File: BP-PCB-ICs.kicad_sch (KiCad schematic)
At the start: 40 parts, among them Q1 SSM6K514NU,LF, Q2 SSM6K514NU,LF, Q3 SSM6K514NU,LF, Q4 SSM6K514NU,LF, Q5 SSM6K514NU,LF, Q6 SSM6K514NU,LF, U1 LTC4361CTS8-2TRMPBF, U2 LTC4361CTS8-2TRMPBF, U4 LTC4380IDD-4-PBF, U6 LTC4380IDD-4-PBF

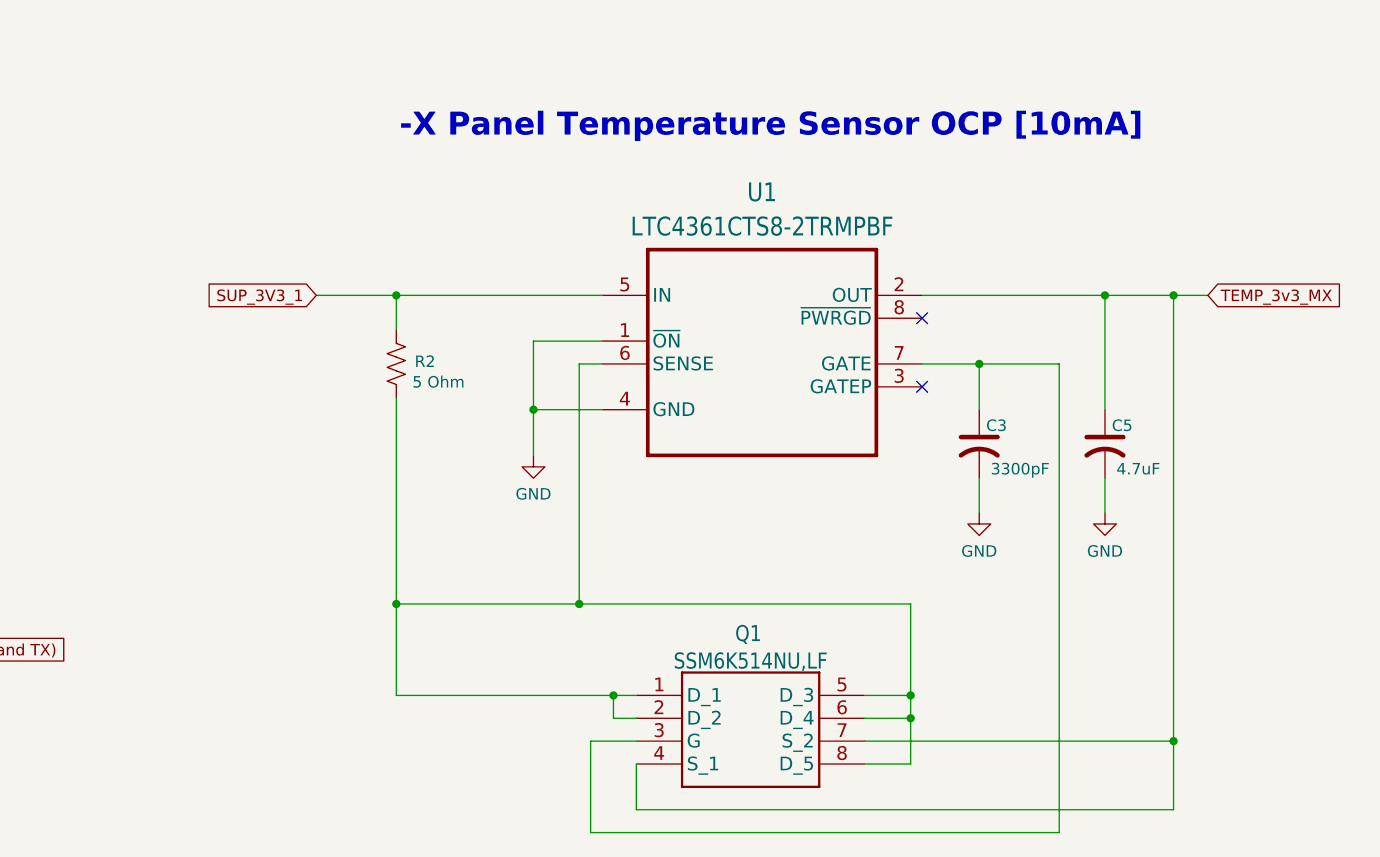
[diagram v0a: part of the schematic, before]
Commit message: -X temp OCP is being shared with BP
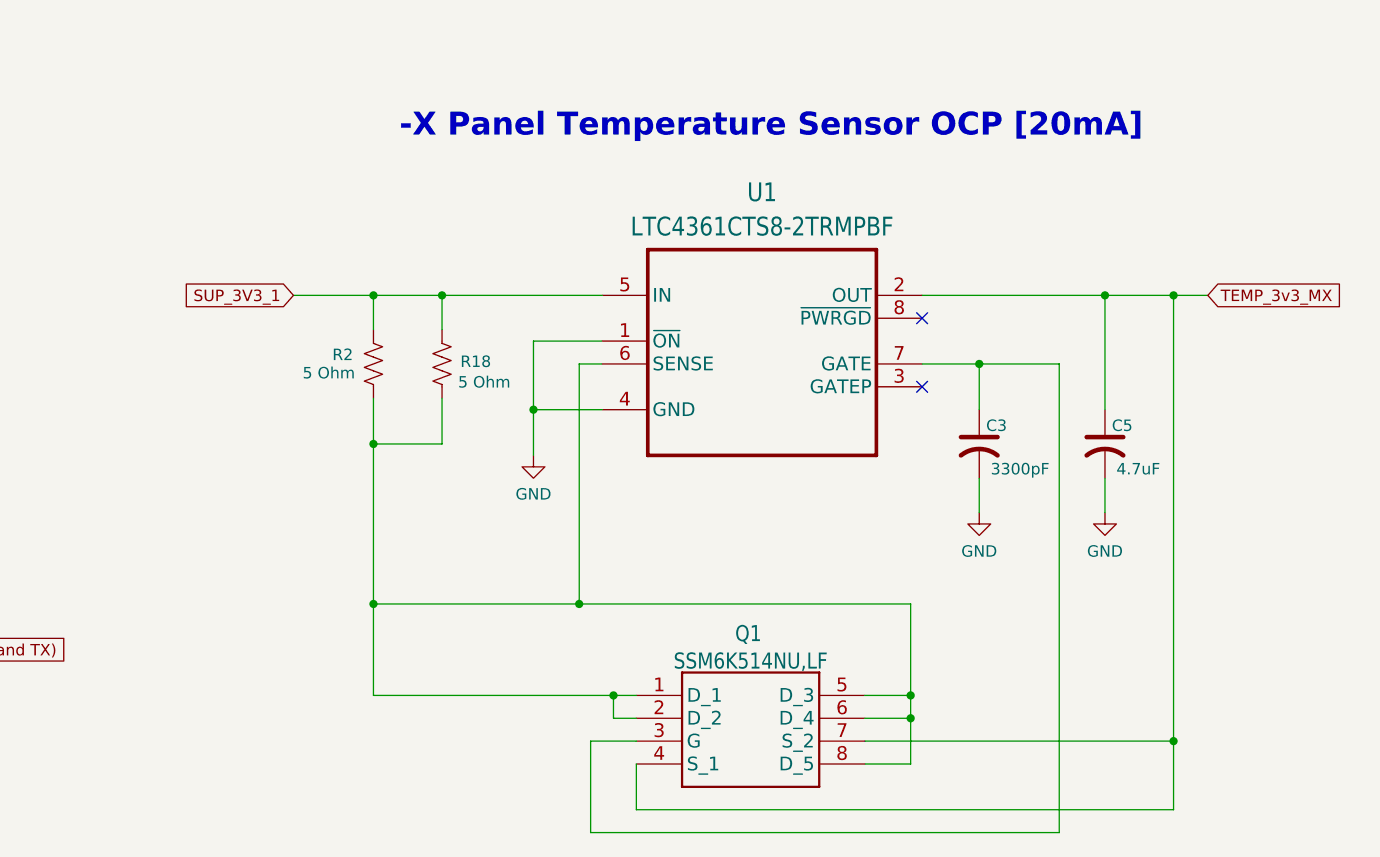
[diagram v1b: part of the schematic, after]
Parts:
- added R18: 5 Ohm, Resistor_SMD:R_0805_2012Metric, symbol Device:R_US
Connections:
- net SUP_3V3_1: now also R18.1
- net at Q1.1 (D_1), Q1.2 (D_2), Q1.5 (D_3)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: now also R18.2
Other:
- note added: "-X Panel Temperature Sensor OCP [20mA]"
- note removed: "-X Panel Temperature Sensor OCP [10mA]"
- moved on the sheet: R2
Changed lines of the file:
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@@
 		)
 	)
-	(text "-X Panel Temperature Sensor OCP [10mA]"
+	(text "-X Panel Temperature Sensor OCP [20mA]"
 		(exclude_from_sim no)
 		(at 329.946 32.004 0)
@@
 	)
 	(junction
+		(at 285.75 85.09)
+		(diameter 0)
+		(color 0 0 0 0)
+	)
+	(junction
 		(at 181.61 201.93)
 		(diameter 0)
@@
 	)
 	(junction
+		(at 293.37 50.8)
+		(diameter 0)
+		(color 0 0 0 0)
+	)
+	(junction
 		(at 345.44 198.12)
 		(diameter 0)
@@
 	)
 	(junction
-		(at 288.29 85.09)
-		(diameter 0)
-		(color 0 0 0 0)
-	)
-	(junction
 		(at 175.26 39.37)
 		(diameter 0)
@@
 	)
 	(junction
+		(at 285.75 50.8)
+		(diameter 0)
+		(color 0 0 0 0)
+	)
+	(junction
 		(at 288.29 153.67)
 		(diameter 0)
@@
 	)
 	(junction
-		(at 288.29 50.8)
-		(diameter 0)
-		(color 0 0 0 0)
-	)
-	(junction
 		(at 140.97 171.45)
 		(diameter 0)
@@
 		(color 0 0 0 0)
 	)
+	(junction
+		(at 285.75 67.31)
+		(diameter 0)
+		(color 0 0 0 0)
+	)
 	(no_connect
 		(at 346.71 60.96)
@@
 	(wire
 		(pts
+			(xy 285.75 50.8) (xy 293.37 50.8)
+		)
+		(stroke
+			(width 0)
+			(type default)
+		)
+	)
+	(wire
+		(pts
 			(xy 55.88 29.21) (xy 55.88 40.64)
 		)
@@
 	(wire
 		(pts
+			(xy 285.75 67.31) (xy 285.75 85.09)
+		)
+		(stroke
+			(width 0)
+			(type default)
+		)
+	)
+	(wire
+		(pts
 			(xy 176.53 151.13) (xy 176.53 156.21)
 		)
@@
 	(wire
 		(pts
-			(xy 288.29 95.25) (xy 312.42 95.25)
+			(xy 285.75 95.25) (xy 312.42 95.25)
 		)
 		(stroke
@@
 	(wire
 		(pts
-			(xy 288.29 85.09) (xy 288.29 95.25)
+			(xy 285.75 85.09) (xy 285.75 95.25)
 		)
 		(stroke
@@
 	(wire
 		(pts
-			(xy 288.29 50.8) (xy 311.15 50.8)
-		)
-		(stroke
-			(width 0)
-			(type default)
-		)
-	)
-	(wire
-		(pts
 			(xy 172.72 41.91) (xy 172.72 48.26)
 		)
@@
 	(wire
 		(pts
-			(xy 279.4 50.8) (xy 288.29 50.8)
+			(xy 276.86 50.8) (xy 285.75 50.8)
 		)
 		(stroke
@@
 	(wire
 		(pts
-			(xy 140.97 153.67) (xy 140.97 171.45)
+			(xy 293.37 62.23) (xy 293.37 67.31)
 		)
 		(stroke
@@
 	(wire
 		(pts
-			(xy 97.79 184.15) (xy 105.41 184.15)
+			(xy 140.97 153.67) (xy 140.97 171.45)
 		)
 		(stroke
@@
 	(wire
 		(pts
-			(xy 308.61 85.09) (xy 288.29 85.09)
+			(xy 97.79 184.15) (xy 105.41 184.15)
 		)
 		(stroke
@@
 	(wire
 		(pts
-			(xy 288.29 50.8) (xy 288.29 54.61)
-		)
-		(stroke
-			(width 0)
-			(type default)
-		)
-	)
-	(wire
-		(pts
 			(xy 181.61 201.93) (xy 176.53 201.93)
 		)
@@
 	(wire
 		(pts
+			(xy 285.75 67.31) (xy 293.37 67.31)
+		)
+		(stroke
+			(width 0)
+			(type default)
+		)
+	)
+	(wire
+		(pts
 			(xy 374.65 203.2) (xy 374.65 153.67)
 		)
@@
 	(wire
 		(pts
-			(xy 288.29 62.23) (xy 288.29 85.09)
+			(xy 285.75 62.23) (xy 285.75 67.31)
 		)
 		(stroke
@@
 	(wire
 		(pts
+			(xy 285.75 50.8) (xy 285.75 54.61)
+		)
+		(stroke
+			(width 0)
+			(type default)
+		)
+	)
+	(wire
+		(pts
 			(xy 144.78 220.98) (xy 143.51 220.98)
 		)
@@
 	(wire
 		(pts
+			(xy 293.37 50.8) (xy 311.15 50.8)
+		)
+		(stroke
+			(width 0)
+			(type default)
+		)
+	)
+	(wire
+		(pts
 			(xy 340.36 100.33) (xy 374.65 100.33)
 		)
@@
 	(wire
 		(pts
+			(xy 285.75 85.09) (xy 308.61 85.09)
+		)
+		(stroke
+			(width 0)
+			(type default)
+		)
+	)
+	(wire
+		(pts
 			(xy 143.51 109.22) (xy 142.24 109.22)
 		)
@@
 	(wire
 		(pts
+			(xy 293.37 54.61) (xy 293.37 50.8)
+		)
+		(stroke
+			(width 0)
+			(type default)
+		)
+	)
+	(wire
+		(pts
 			(xy 142.24 106.68) (xy 143.51 106.68)
 		)
@@
 	(global_label "SUP_3V3_1"
 		(shape input)
-		(at 279.4 50.8 180)
+		(at 276.86 50.8 180)
 		(fields_autoplaced yes)
 		(effects
@@
 		)
 		(property "Intersheetrefs" "${INTERSHEET_REFS}"
-			(at 265.9525 50.8 0)
+			(at 263.4125 50.8 0)
 			(effects
 				(font
@@
 	(symbol
 		(lib_id "Device:R_US")
-		(at 288.29 58.42 0)
+		(at 285.75 58.42 0)
 		(unit 1)
 		(exclude_from_sim no)
@@
 		(dnp no)
 		(property "Reference" "R2"
-			(at 290.322 58.166 0)
+			(at 281.178 57.404 0)
 			(effects
 				(font
@@
 		)
 		(property "Value" "5 Ohm"
-			(at 290.068 60.452 0)
+			(at 277.876 59.436 0)
 			(effects
 				(font
@@
 		)
 		(property "Footprint" "Resistor_SMD:R_0805_2012Metric"
-			(at 289.306 58.674 90)
+			(at 286.766 58.674 90)
 			(effects
 				(font
@@
 		)
 		(property "Datasheet" "~"
-			(at 288.29 58.42 0)
+			(at 285.75 58.42 0)
 			(effects
 				(font
@@
 		)
 		(property "Description" "Resistor, US symbol"
-			(at 288.29 58.42 0)
+			(at 285.75 58.42 0)
 			(effects
 				(font
@@
 					(unit 1)
 				)
+			)
+		)
+	)
+	(symbol
+		(lib_id "Device:R_US")
+		(at 293.37 58.42 0)
+		(unit 1)
+		(exclude_from_sim no)
+		(in_bom yes)
+		(on_board yes)
+		(dnp no)
+		(property "Reference" "R18"
+			(at 295.402 58.166 0)
+			(effects
+				(font
+					(size 1.27 1.27)
+				)
+				(justify left)
+			)
+		)
+		(property "Value" "5 Ohm"
+			(at 295.148 60.452 0)
+			(effects
+				(font
+					(size 1.27 1.27)
+				)
+				(justify left)
+			)
+		)
+		(property "Footprint" "Resistor_SMD:R_0805_2012Metric"
+			(at 294.386 58.674 90)
+			(effects
+				(font
+					(size 1.27 1.27)
+				)
+				(hide yes)
+			)
+		)
+		(property "Datasheet" "~"
+			(at 293.37 58.42 0)
+			(effects
+				(font
+					(size 1.27 1.27)
+				)
+				(hide yes)
+			)
+		)
+		(property "Description" "Resistor, US symbol"
+			(at 293.37 58.42 0)
+			(effects
+				(font
+					(size 1.27 1.27)
+				)
+				(hide yes)
+			)
+		)
+		(pin "1"
+		)
+		(pin "2"
+		)
+		(instances
+			(project "BP-PCB-Kicad"
+				(path "/da3a05e5-7f1e-43cd-9425-16ff965529d1/b13c3f99-87b6-43ee-99ee-c97ccd64f2f6"
+					(reference "R18")
+					(unit 1)
+				)

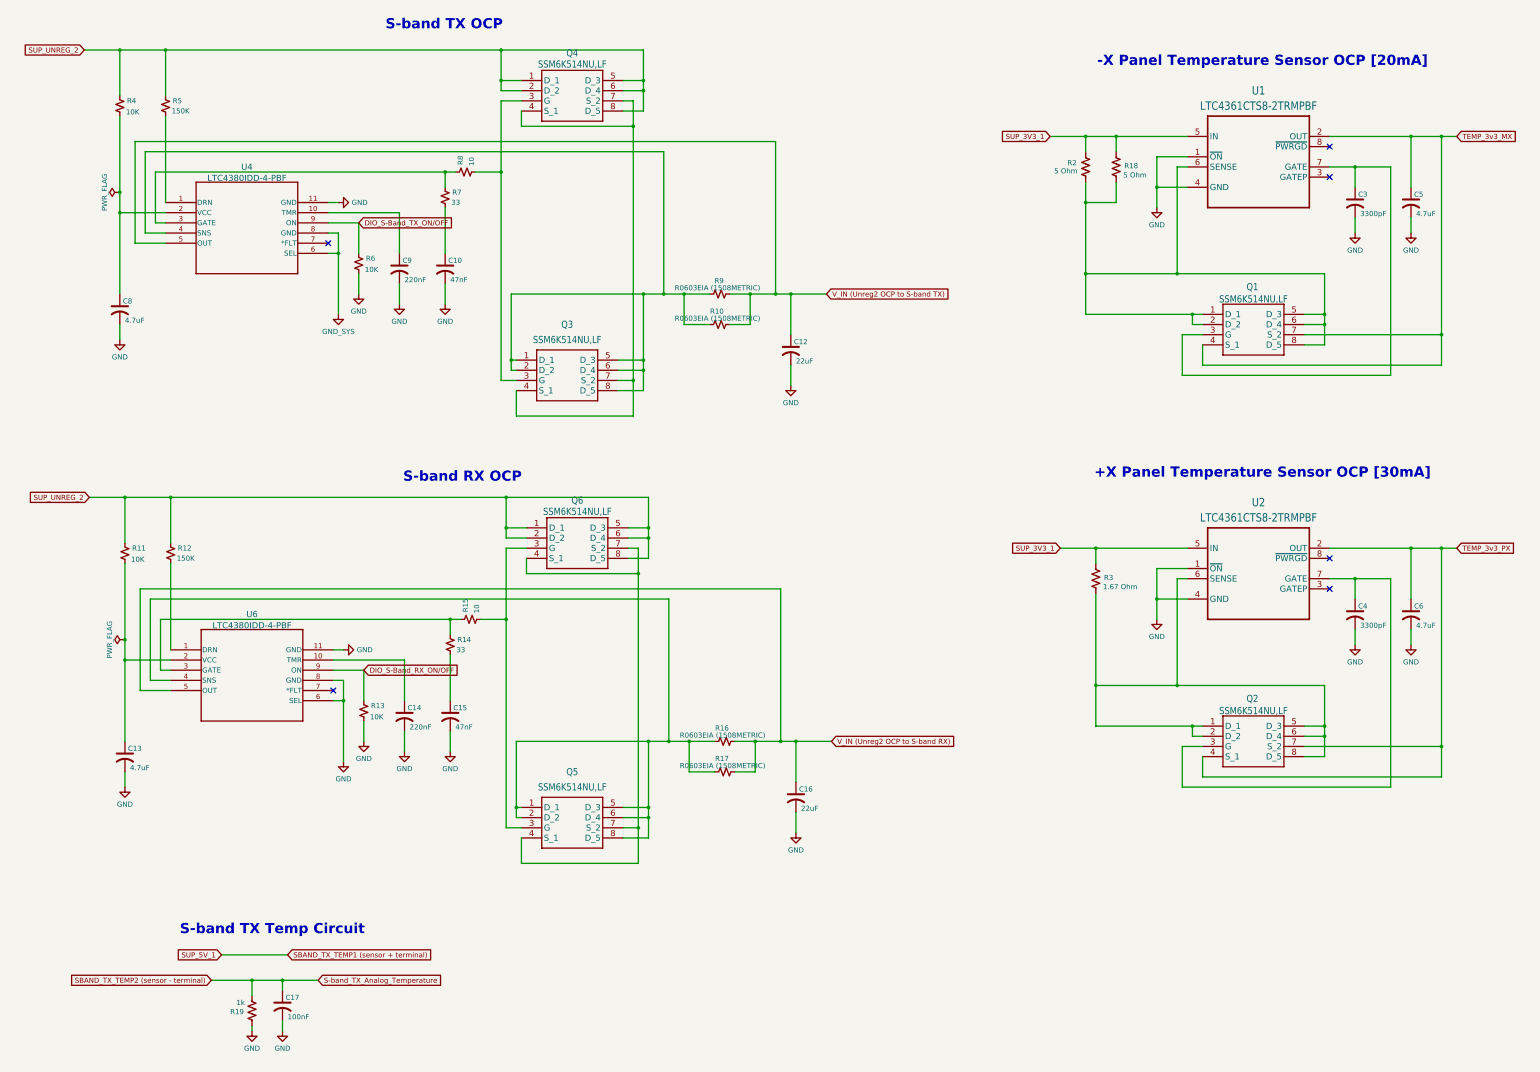
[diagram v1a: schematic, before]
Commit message: PCB layout is syncronized with schematic
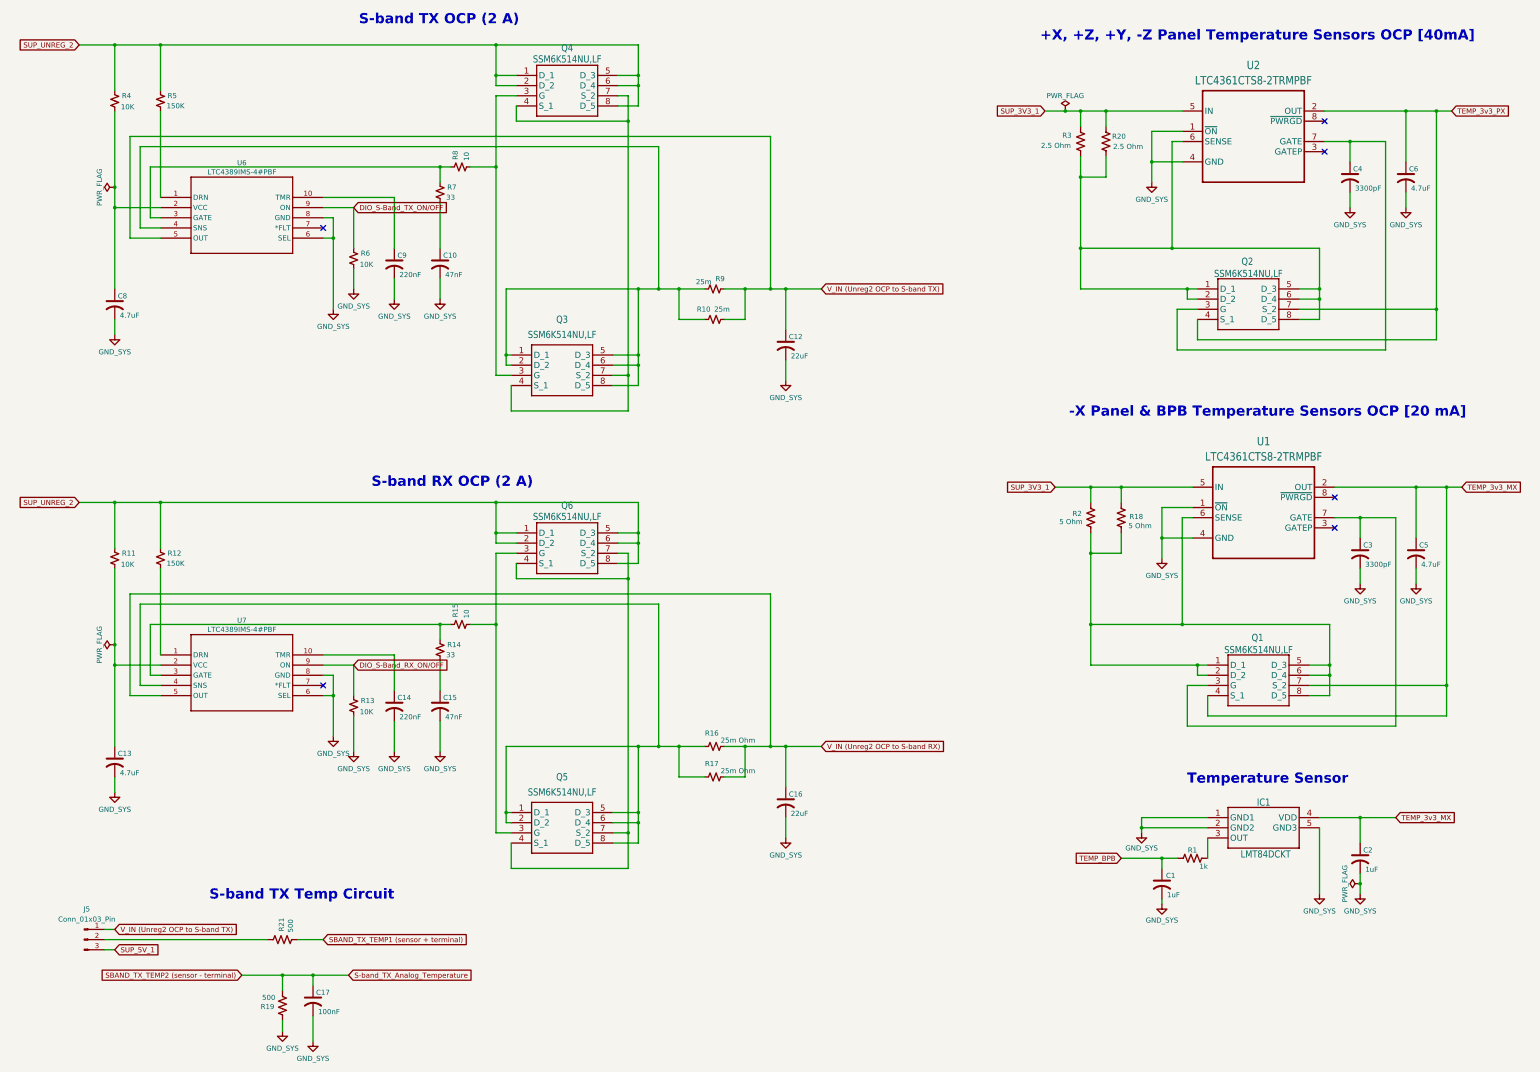
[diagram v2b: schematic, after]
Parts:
- removed U4, U6: LTC4380IDD-4-PBF, Custom-Footprints:LTC4380IDD-4#PBF, symbol Custom-Symbols:LTC4380IDD-4-PBF
- added C1, C2: 1uF, Capacitor_SMD:C_0805_2012Metric, symbol Device:C_US
- added IC1: LMT84DCKT, Custom-Footprints:LMT84DCKT, symbol Custom-Symbols:LMT84DCKT
- added J5: Conn_01x03_Pin, Connector_PinHeader_2.54mm:PinHeader_1x03_P2.54mm_Vertical, symbol Connector:Conn_01x03_Pin
- added R1: 1k, Resistor_SMD:R_0805_2012Metric, symbol Device:R_US
- added R20: 2.5 Ohm, Resistor_SMD:R_0805_2012Metric, symbol Device:R_US
- added R21: 500, Resistor_SMD:R_0805_2012Metric, symbol Device:R_US
- added U6, U7: LTC4389IMS-4#PBF, Custom-Footprints:LTC4380IMS-4#PBF, symbol Custom-Symbols:LTC4380IMS-4#PBF
- R10, R9: value R0603EIA (1508METRIC) -> 25m
- R16, R17: value R0603EIA (1508METRIC) -> 25m Ohm
- R19: value 1k -> 500
- R3: value 1.67 Ohm -> 2.5 Ohm
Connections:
- net GND is gone; now on net GND_SYS: C10.2, C12.2, C13.2, C14.2, C15.2, C16.2, C17.2, C3.2, C4.2, C5.2, C6.2, C8.2, C9.2, R13.2, R19.1, R6.2, U1.1 (~{ON}), U1.4 (GND), U2.1 (~{ON}), U2.4 (GND)
- net  V_IN (Unreg2 OCP to S-band RX): now also U7.5 (OUT)
- net  V_IN (Unreg2 OCP to S-band TX): now also J5.1 (Pin_1), U6.5 (OUT)
- net DIO_S-Band_RX_ON/OFF: now also U7.9 (ON)
- net DIO_S-Band_TX_ON/OFF: now also U6.9 (ON)
- net GND_SYS: now also C1.2, C2.2, IC1.1 (GND1), IC1.2 (GND2), IC1.5 (GND3), U6.6 (SEL), U6.8 (GND), U7.6 (SEL), U7.8 (GND)
- net SBAND_TX_TEMP1 (sensor + terminal) : now also R21.2
- net SUP_3V3_1: now also R20.1
- net TEMP_3v3_MX: now also C2.1, IC1.4 (VDD)
- net at C8.1, R4.2: now also U6.2 (VCC)
- net at R14.1, R15.1: now also U7.3 (GATE)
- net at Q3.1 (D_1), Q3.2 (D_2), Q3.5 (D_3)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: now also U6.4 (SNS)
- net at Q2.1 (D_1), Q2.2 (D_2), Q2.5 (D_3)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: now also R20.2
- net at C13.1, R11.2: now also U7.2 (VCC)
- net at Q5.1 (D_1), Q5.2 (D_2), Q5.5 (D_3)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: now also U7.4 (SNS)
- net at C14.1: now also U7.10 (TMR)
- net at R7.1, R8.1: now also U6.3 (GATE)
- net at R5.2: now also U6.1 (DRN)
- net at R12.2: now also U7.1 (DRN)
- net at C9.1: now also U6.10 (TMR)
- new net: IC1.3 (OUT), R1.2
- new net: J5.2 (Pin_2), R21.1
- new net SUP_5V_1: J5.3 (Pin_3)
- new net TEMP_BPB: C1.1, R1.1
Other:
- note added: "+X, +Z, +Y, -Z Panel Temperature Sensors OCP [40mA]"
- note added: "-X Panel & BPB Temperature Sensors OCP [20 mA]"
- note added: "S-band RX OCP (2 A)"
- note added: "S-band TX OCP (2 A)"
- note added: "Temperature Sensor"
- note removed: "+X Panel Temperature Sensor OCP [30mA]"
- note removed: "-X Panel Temperature Sensor OCP [20mA]"
- note removed: "S-band RX OCP"
- note removed: "S-band TX OCP"
- title: (none) -> BP PCB Ics-1
- moved on the sheet: C10, C12, C13, C14, C15, C16, C17, C3, C4, C5, C6, C8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

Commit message: Microelectronic components placed onto the back of BPB
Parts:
- removed J5: Conn_01x03_Pin, Connector_PinHeader_2.54mm:PinHeader_1x03_P2.54mm_Vertical, symbol Connector:Conn_01x03_Pin
- added D1: BZT52C3V6LP-7, Custom-Footprints:DIO_BZT52C3V6LP-7, symbol Custom-Symbols:BZT52C3V6LP-7
- added R22, R23: 0, Resistor_SMD:R_0805_2012Metric, symbol Device:R_US
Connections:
- net  V_IN (Unreg2 OCP to S-band TX): now also R22.1
- net GND_SYS: now also D1.A
- net S-band_TX_Analog_Temperature: now also D1.C
- net SUP_5V_1: now also R23.1
- net at R21.1: now also R22.2, R23.2
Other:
- moved on the sheet: C17, R19
